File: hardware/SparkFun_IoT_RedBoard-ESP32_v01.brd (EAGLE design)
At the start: 68.6 x 58.4 mm, 213 parts, among them J1 5.5x2.1mm Barrel, J13 QWIIC_RIGHT_ANGLE, J15 MICRO-SD-PUSH-PUSH-EXT-PIN, J2 USB C, J3 USB_SOLDER_PADS, J5 M10NO_SILK, Q1 MBT3904DW1T1, Q11 20V/4.2A/52mΩ/1.4W, Q13 20V/4.2A/52mΩ/1.4W, Q3 20V/4.2A/52mΩ/1.4W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

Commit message: Increase resistors on perfect diodes to reduce quiescent current
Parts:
- R17, R19, R24, R26: value 10k -> 100k
- R18, R20, R25, R27: value 47k -> 1M
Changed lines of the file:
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@@
 <drawing>
 <settings>
-<setting alwaysvectorfont="no"/>
+<setting alwaysvectorfont="yes"/>
 <setting keepoldvectorfont="yes"/>
 <setting verticaltext="up"/>
@@
 <attribute name="VALUE" x="29.21" y="21.971" size="0.6096" layer="27" font="vector" ratio="20" rot="R180" align="top-center"/>
 </element>
-<element name="R17" library="SparkFun-Resistors" package="0603" value="10k" x="36.83" y="12.7" smashed="yes" rot="R180">
+<element name="R17" library="SparkFun-Resistors" package="0603" value="100k" x="36.83" y="12.7" smashed="yes" rot="R180">
 <attribute name="NAME" x="36.83" y="11.938" size="0.6096" layer="25" font="vector" ratio="20" rot="R180" align="bottom-center"/>
-<attribute name="PROD_ID" value="RES-00824" x="44.45" y="13.97" size="1.778" layer="27" rot="R180" display="off"/>
-<attribute name="VALUE" x="36.83" y="13.462" size="0.6096" layer="27" font="vector" ratio="20" rot="R180" align="top-center"/>
-</element>
-<element name="R18" library="SparkFun-Resistors" package="0603" value="47k" x="40.64" y="12.7" smashed="yes" rot="R180">
+<attribute name="PROD_ID" value="RES-07828" x="44.45" y="13.97" size="1.778" layer="27" rot="R180" display="off"/>
+<attribute name="VALUE" value="100k" x="36.83" y="13.462" size="0.6096" layer="27" font="vector" ratio="20" rot="R180" align="top-center"/>
+</element>
+<element name="R18" library="SparkFun-Resistors" package="0603" value="1M" x="40.64" y="12.7" smashed="yes" rot="R180">
 <attribute name="NAME" x="40.64" y="11.938" size="0.6096" layer="25" font="vector" ratio="20" rot="R180" align="bottom-center"/>
-<attribute name="PROD_ID" value="RES-07871" x="40.64" y="12.7" size="1.778" layer="27" rot="R180" display="off"/>
-<attribute name="VALUE" x="40.64" y="13.462" size="0.6096" layer="27" font="vector" ratio="20" rot="R180" align="top-center"/>
+<attribute name="PROD_ID" value="RES-07868" x="40.64" y="12.7" size="1.778" layer="27" rot="R180" display="off"/>
+<attribute name="VALUE" value="1M" x="40.64" y="13.462" size="0.6096" layer="27" font="vector" ratio="20" rot="R180" align="top-center"/>
 </element>
 <element name="Q8" library="SparkFun-DiscreteSemi" package="SOT363_PHILIPS" package3d_urn="urn:adsk.eagle:package:29757/2" value="" x="33.02" y="24.13" smashed="yes" rot="R270">
@@
 <attribute name="VALUE" x="29.21" y="25.781" size="0.6096" layer="27" font="vector" ratio="20" rot="R180" align="top-center"/>
 </element>
-<element name="R19" library="SparkFun-Resistors" package="0603" value="10k" x="36.83" y="24.13" smashed="yes" rot="R180">
+<element name="R19" library="SparkFun-Resistors" package="0603" value="100k" x="36.83" y="24.13" smashed="yes" rot="R180">
 <attribute name="NAME" x="36.83" y="23.368" size="0.6096" layer="25" font="vector" ratio="20" rot="R180" align="bottom-center"/>
-<attribute name="PROD_ID" value="RES-00824" x="40.64" y="40.64" size="1.778" layer="27" rot="R180" display="off"/>
-<attribute name="VALUE" x="36.83" y="24.892" size="0.6096" layer="27" font="vector" ratio="20" rot="R180" align="top-center"/>
-</element>
-<element name="R20" library="SparkFun-Resistors" package="0603" value="47k" x="36.83" y="22.225" smashed="yes" rot="R180">
+<attribute name="PROD_ID" value="RES-07828" x="40.64" y="40.64" size="1.778" layer="27" rot="R180" display="off"/>
+<attribute name="VALUE" value="100k" x="36.83" y="24.892" size="0.6096" layer="27" font="vector" ratio="20" rot="R180" align="top-center"/>
+</element>
+<element name="R20" library="SparkFun-Resistors" package="0603" value="1M" x="36.83" y="22.225" smashed="yes" rot="R180">
 <attribute name="NAME" x="36.83" y="21.463" size="0.6096" layer="25" font="vector" ratio="20" rot="R180" align="bottom-center"/>
-<attribute name="PROD_ID" value="RES-07871" x="44.45" y="42.545" size="1.778" layer="27" rot="R180" display="off"/>
-<attribute name="VALUE" x="36.83" y="22.987" size="0.6096" layer="27" font="vector" ratio="20" rot="R180" align="top-center"/>
+<attribute name="PROD_ID" value="RES-07868" x="44.45" y="42.545" size="1.778" layer="27" rot="R180" display="off"/>
+<attribute name="VALUE" value="1M" x="36.83" y="22.987" size="0.6096" layer="27" font="vector" ratio="20" rot="R180" align="top-center"/>
 </element>
 <element name="C13" library="SparkFun-Capacitors" package="0603" value="0.1uF" x="8.89" y="2.032" smashed="yes" rot="R270">
@@
 <attribute name="VALUE" x="29.21" y="14.859" size="0.6096" layer="27" font="vector" ratio="20" align="top-center"/>
 </element>
-<element name="R24" library="SparkFun-Resistors" package="0603" value="10k" x="36.83" y="20.32" smashed="yes" rot="R180">
+<element name="R24" library="SparkFun-Resistors" package="0603" value="100k" x="36.83" y="20.32" smashed="yes" rot="R180">
 <attribute name="NAME" x="36.83" y="19.558" size="0.6096" layer="25" font="vector" ratio="20" rot="R180" align="bottom-center"/>
-<attribute name="PROD_ID" value="RES-00824" x="46.99" y="21.59" size="1.778" layer="27" rot="R180" display="off"/>
-<attribute name="VALUE" x="36.83" y="21.082" size="0.6096" layer="27" font="vector" ratio="20" rot="R180" align="top-center"/>
-</element>
-<element name="R25" library="SparkFun-Resistors" package="0603" value="47k" x="36.83" y="18.415" smashed="yes" rot="R180">
+<attribute name="PROD_ID" value="RES-07828" x="46.99" y="21.59" size="1.778" layer="27" rot="R180" display="off"/>
+<attribute name="VALUE" value="100k" x="36.83" y="21.082" size="0.6096" layer="27" font="vector" ratio="20" rot="R180" align="top-center"/>
+</element>
+<element name="R25" library="SparkFun-Resistors" package="0603" value="1M" x="36.83" y="18.415" smashed="yes" rot="R180">
 <attribute name="NAME" x="36.83" y="17.653" size="0.6096" layer="25" font="vector" ratio="20" rot="R180" align="bottom-center"/>
-<attribute name="PROD_ID" value="RES-07871" x="36.83" y="18.415" size="1.778" layer="27" rot="R180" display="off"/>
-<attribute name="VALUE" x="36.83" y="19.177" size="0.6096" layer="27" font="vector" ratio="20" rot="R180" align="top-center"/>
+<attribute name="PROD_ID" value="RES-07868" x="36.83" y="18.415" size="1.778" layer="27" rot="R180" display="off"/>
+<attribute name="VALUE" value="1M" x="36.83" y="19.177" size="0.6096" layer="27" font="vector" ratio="20" rot="R180" align="top-center"/>
 </element>
 <element name="Q12" library="SparkFun-DiscreteSemi" package="SOT363_PHILIPS" package3d_urn="urn:adsk.eagle:package:29757/2" value="" x="33.02" y="16.51" smashed="yes" rot="R270">
@@
 <attribute name="VALUE" x="29.21" y="11.049" size="0.6096" layer="27" font="vector" ratio="20" align="top-center"/>
 </element>
-<element name="R26" library="SparkFun-Resistors" package="0603" value="10k" x="36.83" y="16.51" smashed="yes" rot="R180">
+<element name="R26" library="SparkFun-Resistors" package="0603" value="100k" x="36.83" y="16.51" smashed="yes" rot="R180">
 <attribute name="NAME" x="36.83" y="15.748" size="0.6096" layer="25" font="vector" ratio="20" rot="R180" align="bottom-center"/>
-<attribute name="PROD_ID" value="RES-00824" x="40.64" y="33.02" size="1.778" layer="27" rot="R180" display="off"/>
-<attribute name="VALUE" x="36.83" y="17.272" size="0.6096" layer="27" font="vector" ratio="20" rot="R180" align="top-center"/>
-</element>
-<element name="R27" library="SparkFun-Resistors" package="0603" value="47k" x="36.83" y="14.605" smashed="yes" rot="R180">
+<attribute name="PROD_ID" value="RES-07828" x="40.64" y="33.02" size="1.778" layer="27" rot="R180" display="off"/>
+<attribute name="VALUE" value="100k" x="36.83" y="17.272" size="0.6096" layer="27" font="vector" ratio="20" rot="R180" align="top-center"/>
+</element>
+<element name="R27" library="SparkFun-Resistors" package="0603" value="1M" x="36.83" y="14.605" smashed="yes" rot="R180">
 <attribute name="NAME" x="36.83" y="13.843" size="0.6096" layer="25" font="vector" ratio="20" rot="R180" align="bottom-center"/>
-<attribute name="PROD_ID" value="RES-07871" x="44.45" y="34.925" size="1.778" layer="27" rot="R180" display="off"/>
-<attribute name="VALUE" x="36.83" y="15.367" size="0.6096" layer="27" font="vector" ratio="20" rot="R180" align="top-center"/>
+<attribute name="PROD_ID" value="RES-07868" x="44.45" y="34.925" size="1.778" layer="27" rot="R180" display="off"/>
+<attribute name="VALUE" value="1M" x="36.83" y="15.367" size="0.6096" layer="27" font="vector" ratio="20" rot="R180" align="top-center"/>
 </element>
 <element name="U6" library="SparkFun-IC-Power" package="DFN-8" value="MAX17048" x="17.78" y="10.16" smashed="yes">

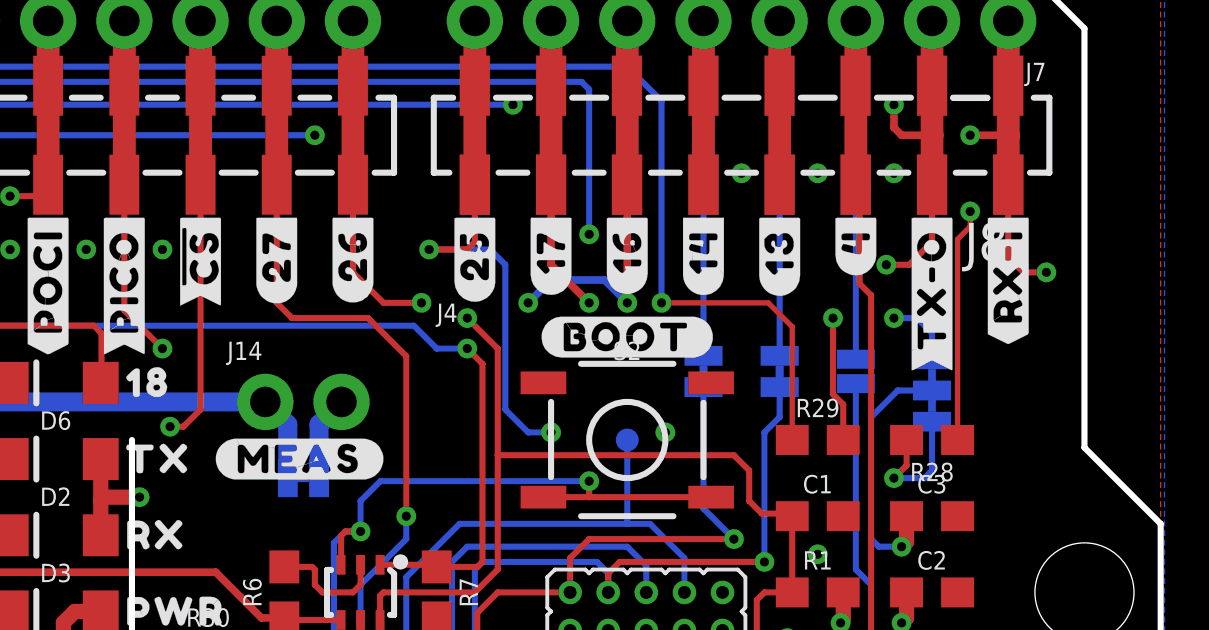
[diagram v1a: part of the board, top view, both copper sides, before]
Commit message: Update cosmetic components and silk
Change power LED to red
Change charge LED to yellow
Change green/yellow LED resistors to 1k
Change red LED resistor to 2.2k
Update some top pin silk labels to include pin numbers
Fix RX silk to be "RX-0" instead of "RX-1"
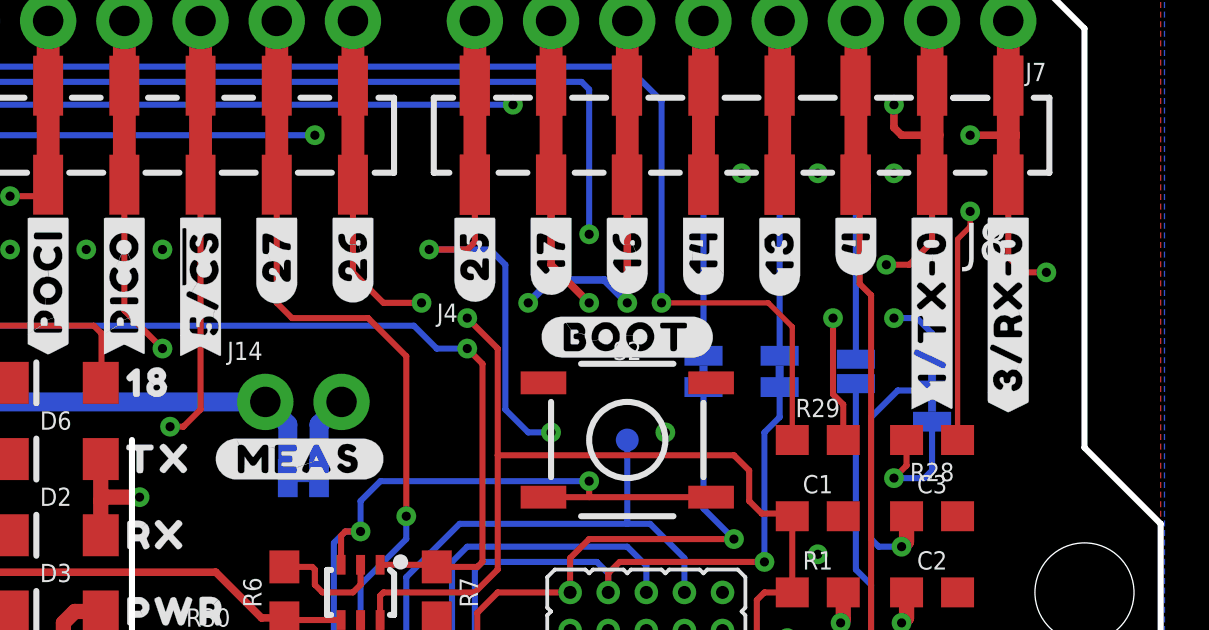
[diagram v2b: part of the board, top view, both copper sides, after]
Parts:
- removed U$11: (no value), output-ESP32:##CS##28
- removed U$64: (no value), output-ESP32:#1#TX#O#32321869
- removed U$65: (no value), output-ESP32:##ALERT##4#321866
- added U$102: (no value), output:#4##ALERT##0
- added U$104: (no value), output:#1#TX#0#0
- added U$105: (no value), output:#1#TX#0#2
- D4: value RED -> YELLOW
- D5: value PWR -> GREEN
- R4, R5: value 4.7k -> 1k
- R8: value 10k -> 2.2k
- U$24: device output-ESP32:#TX#O#0 -> output:#3#RX#0#4
- U$25: device output-ESP32:#RX#I#1 -> output:#3#RX#0#0
- U$63: device output-ESP32:#3#RX#I#32321869 -> output:#5##CS##0
- moved U$63 27.5 mm to (36.6, 50.9), flipped to the top
- moved U$24 6.25 mm to (63.5, 56.6), flipped to the bottom
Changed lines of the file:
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@@
 <attribute name="VALUE" x="16.764" y="57.15" size="0.6096" layer="27" font="vector" ratio="15"/>
 </element>
-<element name="R5" library="SparkFun-Resistors" package="0603" value="4.7k" x="26.67" y="40.005" smashed="yes">
+<element name="R5" library="SparkFun-Resistors" package="0603" value="1k" x="26.67" y="40.005" smashed="yes">
 <attribute name="NAME" x="25.781" y="40.767" size="0.4064" layer="25" font="vector"/>
-<attribute name="PROD_ID" value="RES-07857" x="10.16" y="31.115" size="1.778" layer="27" font="vector" ratio="15" display="off"/>
-<attribute name="VALUE" value="4.7k" x="29.972" y="40.386" size="0.6096" layer="27" font="vector" ratio="15" rot="R180"/>
+<attribute name="PROD_ID" value="RES-07856" x="10.16" y="31.115" size="1.778" layer="27" font="vector" ratio="15" display="off"/>
+<attribute name="VALUE" value="1k" x="29.972" y="40.386" size="0.6096" layer="27" font="vector" ratio="15" rot="R180"/>
 </element>
 <element name="C7" library="SparkFun-Capacitors" package="0603" value="0.1uF" x="15.24" y="48.768" smashed="yes" rot="R90">
@@
 <attribute name="VALUE" x="14.605" y="47.752" size="0.6096" layer="27" font="vector" ratio="15" rot="R90"/>
 </element>
-<element name="R4" library="SparkFun-Resistors" package="0603" value="4.7k" x="26.67" y="42.545" smashed="yes">
+<element name="R4" library="SparkFun-Resistors" package="0603" value="1k" x="26.67" y="42.545" smashed="yes">
 <attribute name="NAME" x="25.781" y="43.307" size="0.4064" layer="25" font="vector"/>
-<attribute name="PROD_ID" value="RES-07857" x="3.81" y="26.035" size="1.778" layer="27" font="vector" ratio="15" display="off"/>
-<attribute name="VALUE" value="4.7k" x="29.972" y="42.799" size="0.6096" layer="27" font="vector" ratio="15" rot="R180"/>
+<attribute name="PROD_ID" value="RES-07856" x="3.81" y="26.035" size="1.778" layer="27" font="vector" ratio="15" display="off"/>
+<attribute name="VALUE" value="1k" x="29.972" y="42.799" size="0.6096" layer="27" font="vector" ratio="15" rot="R180"/>
 </element>
 <element name="J2" library="SparkFun-Connectors" package="USB-C-16P-2LAYER-PADS" value="USB C" x="6.35" y="41.91" smashed="yes" rot="R270">
@@
 <attribute name="VALUE" x="12.192" y="17.78" size="0.6096" layer="27" font="vector" ratio="20" rot="R90" align="top-center"/>
 </element>
-<element name="D4" library="SparkFun-LED" package="LED-1206-HIDDENSILK" value="RED" x="31.75" y="34.925" smashed="yes" rot="R180">
+<element name="D4" library="SparkFun-LED" package="LED-1206-HIDDENSILK" value="YELLOW" x="31.75" y="34.925" smashed="yes" rot="R180">
 <attribute name="NAME" x="31.75" y="33.9725" size="0.6096" layer="25" font="vector" ratio="20" rot="R180" align="bottom-center"/>
-<attribute name="PROD_ID" value="DIO-09912" x="52.07" y="40.005" size="1.778" layer="27" rot="R180" display="off"/>
-<attribute name="VALUE" x="31.75" y="35.8775" size="0.6096" layer="27" font="vector" ratio="20" rot="R180" align="top-center"/>
+<attribute name="PROD_ID" value="DIO-09909" x="52.07" y="40.005" size="1.778" layer="27" rot="R180" display="off"/>
+<attribute name="VALUE" value="YELLOW" x="31.75" y="35.8775" size="0.6096" layer="27" font="vector" ratio="20" rot="R180" align="top-center"/>
 </element>
 <element name="Q10" library="SparkFun-DiscreteSemi" package="SOT363_PHILIPS" package3d_urn="urn:adsk.eagle:package:29757/2" value="" x="33.02" y="20.32" smashed="yes" rot="R270">
@@
 <attribute name="VALUE" x="37.465" y="42.418" size="0.6096" layer="27" font="vector" ratio="20"/>
 </element>
-<element name="R8" library="SparkFun-Resistors" package="0603" value="10k" x="26.67" y="37.465" smashed="yes">
+<element name="R8" library="SparkFun-Resistors" package="0603" value="2.2k" x="26.67" y="37.465" smashed="yes">
 <attribute name="NAME" x="26.67" y="38.227" size="0.6096" layer="25" font="vector" ratio="20" align="bottom-center"/>
-<attribute name="PROD_ID" value="RES-00824" x="26.67" y="41.275" size="1.778" layer="27" display="off"/>
-<attribute name="VALUE" x="26.67" y="36.703" size="0.6096" layer="27" font="vector" ratio="20" align="top-center"/>
-</element>
-<element name="D5" library="SparkFun-LED" package="LED-1206-HIDDENSILK" value="PWR" x="31.75" y="37.465" smashed="yes" rot="R180">
+<attribute name="PROD_ID" value="RES-08272" x="26.67" y="41.275" size="1.778" layer="27" display="off"/>
+<attribute name="VALUE" value="2.2k" x="26.67" y="36.703" size="0.6096" layer="27" font="vector" ratio="20" align="top-center"/>
+</element>
+<element name="D5" library="SparkFun-LED" package="LED-1206-HIDDENSILK" value="GREEN" x="31.75" y="37.465" smashed="yes" rot="R180">
 <attribute name="NAME" x="31.75" y="36.5125" size="0.6096" layer="25" font="vector" ratio="20" rot="R180" align="bottom-center"/>
-<attribute name="PROD_ID" value="DIO-00862" x="31.75" y="41.275" size="1.778" layer="27" rot="R180" display="off"/>
-<attribute name="VALUE" x="31.75" y="38.4175" size="0.6096" layer="27" font="vector" ratio="20" rot="R180" align="top-center"/>
+<attribute name="PROD_ID" value="DIO-09912" x="31.75" y="41.275" size="1.778" layer="27" rot="R180" display="off"/>
 </element>
 <element name="LOGO1" library="SparkFun-Aesthetics" package="SFE_LOGO_NAME_.1" value="SFE_LOGO_NAME.1_INCH" x="48.895" y="13.335" smashed="yes"/>
@@
 <element name="U$9" library="output-ESP32" package="#PICO#29" value="" x="34.036" y="50.927" smashed="yes" rot="R90"/>
 <element name="U$10" library="output-ESP32" package="1836" value="" x="33.401" y="45.085" smashed="yes"/>
-<element name="U$11" library="output-ESP32" package="##CS##28" value="" x="36.576" y="50.927" smashed="yes" rot="R90"/>
 <element name="U$12" library="output-ESP32" package="#27#27" value="" x="39.116" y="50.927" smashed="yes" rot="R90"/>
 <element name="U$13" library="output-ESP32" package="#26#26" value="" x="41.656" y="50.927" smashed="yes" rot="R90"/>
@@
 <element name="U$22" library="output-ESP32" package="#13#5" value="" x="55.88" y="50.927" smashed="yes" rot="R90"/>
 <element name="U$23" library="output-ESP32" package="#4#2" value="" x="58.42" y="50.927" smashed="yes" rot="R90"/>
-<element name="U$24" library="output-ESP32" package="#TX#O#0" value="" x="60.96" y="50.927" smashed="yes" rot="R90"/>
-<element name="U$25" library="output-ESP32" package="#RX#I#1" value="" x="63.5" y="50.927" smashed="yes" rot="R90"/>
 <element name="U$26" library="output-ESP32" package="#RESET#1842" value="" x="8.89" y="49.657" smashed="yes"/>
 <element name="U$27" library="output-ESP32" package="#BOOT#1841" value="" x="50.8" y="46.609" smashed="yes"/>
@@
 <element name="U$61" library="output-ESP32" package="##RESET##321864" value="" x="33.02" y="1.778" smashed="yes" rot="MR90"/>
 <element name="U$62" library="output-ESP32" package="#IOREF#321865" value="" x="30.48" y="1.778" smashed="yes" rot="MR90"/>
-<element name="U$63" library="output-ESP32" package="#3#RX#I#32321869" value="" x="63.5" y="56.642" smashed="yes" rot="MR90"/>
-<element name="U$64" library="output-ESP32" package="#1#TX#O#32321869" value="" x="60.96" y="56.642" smashed="yes" rot="MR90"/>
 <element name="U$66" library="output-ESP32" package="#13#TCK#32321869" value="" x="55.88" y="56.642" smashed="yes" rot="MR90"/>
 <element name="U$67" library="output-ESP32" package="#14#TMS#32321869" value="" x="53.34" y="56.642" smashed="yes" rot="MR90"/>
@@
 <element name="U$96" library="output-ESP32" package="INPUT_ONLY321867" value="" x="59.69" y="12.446" smashed="yes"/>
 <element name="U$97" library="output-ESP32" package="INPUT_ONLY321867" value="" x="59.69" y="10.922" smashed="yes" rot="MR0"/>
-<element name="U$65" library="output-ESP32" package="##ALERT##4#321866" value="" x="58.42" y="56.515" smashed="yes" rot="MR90"/>
 <element name="TP1" library="SparkFun-Connectors" package="PAD.03X.03" value="TEST-POINT3" x="50.8" y="43.18" smashed="yes" rot="MR0"/>
 <element name="U$95" library="output-ESP32" package="TP1321868" value="" x="50.8" y="45.212" smashed="yes" rot="MR90"/>
@@
 <attribute name="VALUE" x="36.83" y="35.433" size="0.6096" layer="27" font="vector" ratio="20" align="top-center"/>
 </element>
+<element name="U$25" library="output" package="#3#RX#0#0" value="" x="63.5" y="50.927" smashed="yes" rot="R90"/>
+<element name="U$104" library="output" package="#1#TX#0#0" value="" x="60.96" y="50.927" smashed="yes" rot="R90"/>
+<element name="U$102" library="output" package="#4##ALERT##0" value="" x="58.42" y="56.642" smashed="yes" rot="MR90"/>
+<element name="U$24" library="output" package="#3#RX#0#4" value="" x="63.5" y="56.642" smashed="yes" rot="MR90"/>
+<element name="U$105" library="output" package="#1#TX#0#2" value="" x="60.96" y="56.642" smashed="yes" rot="MR90"/>
+<element name="U$63" library="output" package="#5##CS##0" value="" x="36.576" y="50.927" smashed="yes" rot="R90"/>
 </elements>
 <signals>
